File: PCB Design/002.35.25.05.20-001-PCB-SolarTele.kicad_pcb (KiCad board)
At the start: 2 copper layers, 126.7 x 46 mm, 38 parts, among them J1 Screw_Terminal_01x08, J2 Conn_01x01, J3 SMA, J4 SMA, J5 SMA, J6 SMA, J7 SMA, J8 SMA, U1 L7815, U2 L7805, U3 ADL5902ACPZ-R7, U4 LM358

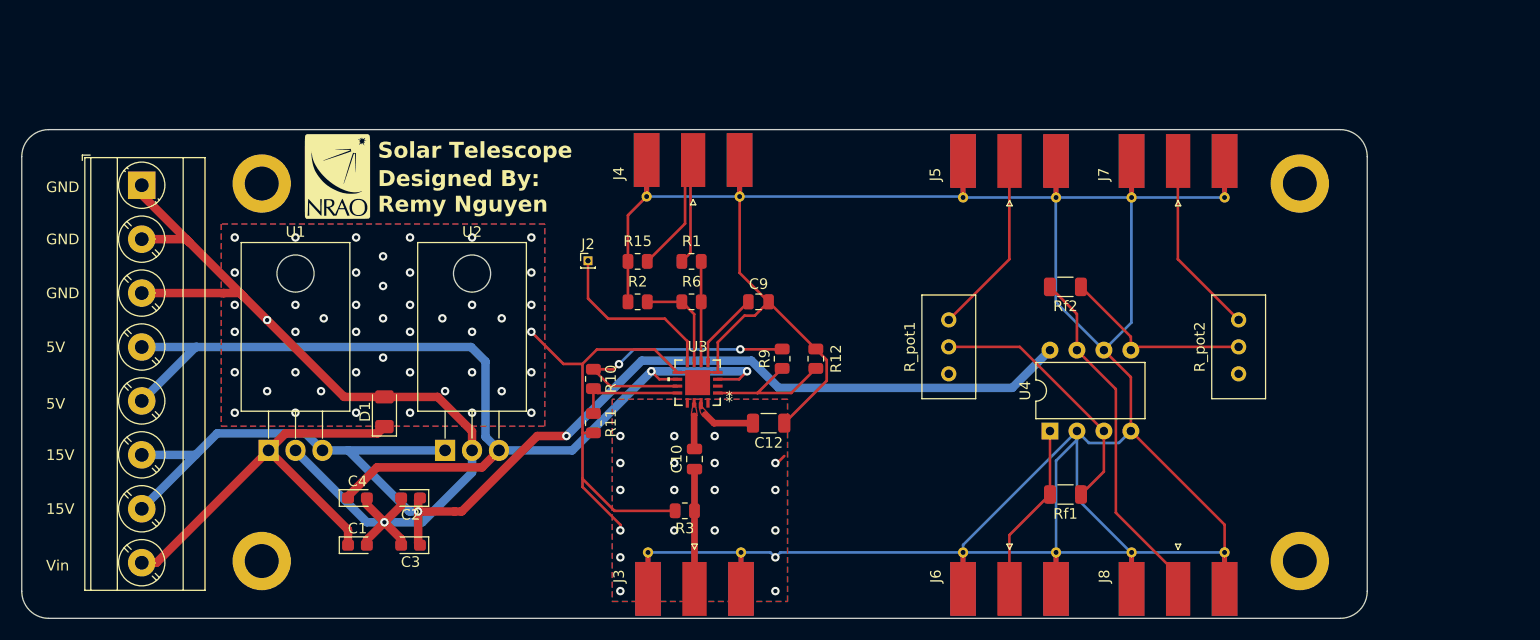
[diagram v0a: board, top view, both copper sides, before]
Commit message: Fixed SMA pad thickness
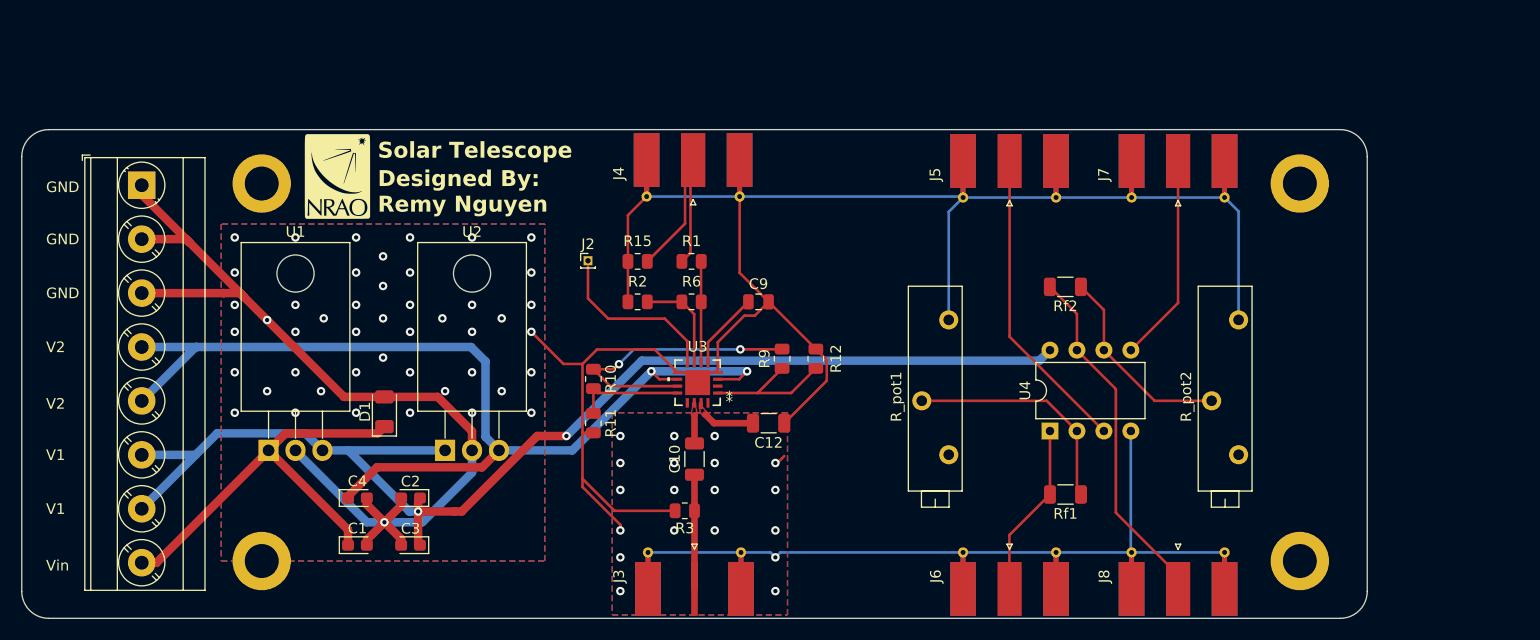
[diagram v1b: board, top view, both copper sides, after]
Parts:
- C10: footprint Capacitor_SMD:C_0805_2012Metric -> Capacitor_SMD:C_1206_3216Metric
- R_pot1, R_pot2: footprint Potentiometer_THT:Potentiometer_Bourns_3296W_Vertical -> Potentiometer_THT:Potentiometer_Bourns_3006P_Horizontal
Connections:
- R_pot1 pad 1: Net-(J5-In) -> GND
- R_pot1 pad 2: Net-(U4A-+) -> Net-(U4A--)
- R_pot2 pad 1: Net-(J7-In) -> GND
- R_pot2 pad 2: Net-(U4B-+) -> Net-(U4B--)
- Rf1 pad 1: Net-(U4A-+) -> Net-(U4A--)
- Rf2 pad 1: Net-(U4B-+) -> Net-(U4B--)
- U4 pad 2: GND -> Net-(U4A--)
- U4 pad 3: Net-(U4A-+) -> Net-(J5-In)
- U4 pad 5: Net-(U4B-+) -> Net-(J7-In)
- U4 pad 6: GND -> Net-(U4B--)
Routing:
- net GND: track 401.9 -> 334.2 mm
- net Net-(U4A-+): track 24.8 -> 0.00 mm
- net Net-(U4A--): track 0.00 -> 21.9 mm
- net Net-(U4B--): track 0.00 -> 19.0 mm
- net Net-(U4B-+): track 18.2 -> 0.00 mm
- net Net-(J5-In): track 17.3 -> 29.1 mm
- net Net-(J7-In): track 17.3 -> 19.7 mm
- net +15VDC: track 121.6 -> 119.5 mm
- net RFIN: track 11.3 -> 10.8 mm
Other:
- board text added: "0"
- board text added: "0 mm"
- board text added: "0.0037"
- board text added: "0.01 mm"
- board text added: "0.03556 mm"
- board text added: "0.762 mm"
- board text added: "1"
- board text added: "1.1"
- board text added: "3.3"
- board text added: "3.66"
- board text added: "B.Cu"
- board text added: "B.Mask"
- board text added: "B.Paste"
- board text added: "B.Silkscreen"
- board text added: "Bottom Silk Screen"
- board text added: "Bottom Solder Mask"
- board text added: "Bottom Solder Paste"
- board text added: "Color"
- board text added: "Dielectric 1"
- board text added: "Epsilon R"
- board text added: "F.Cu"
- board text added: "F.Mask"
- board text added: "F.Paste"
- board text added: "F.Silkscreen"
- board text added: "FR4 natural"
- board text added: "Green"
- board text added: "Layer Name"
- board text added: "Liquid Ink"
- board text added: "Liquid Photo"
- board text added: "Loss Tangent"
- board text added: "Material"
- board text added: "RO4350B"
- board text added: "Thickness (mm)"
- board text added: "Top Silk Screen"
- board text added: "Top Solder Mask"
- board text added: "Top Solder Paste"
- board text added: "Type"
- board text added: "V1"
- board text added: "V2"
- board text added: "White"
- board text added: "copper"
- board text added: "core"
- board text removed: "15V"
- board text removed: "5V"
- board text removed: "D"

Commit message: PCB updated to Revision B, see changelog for details
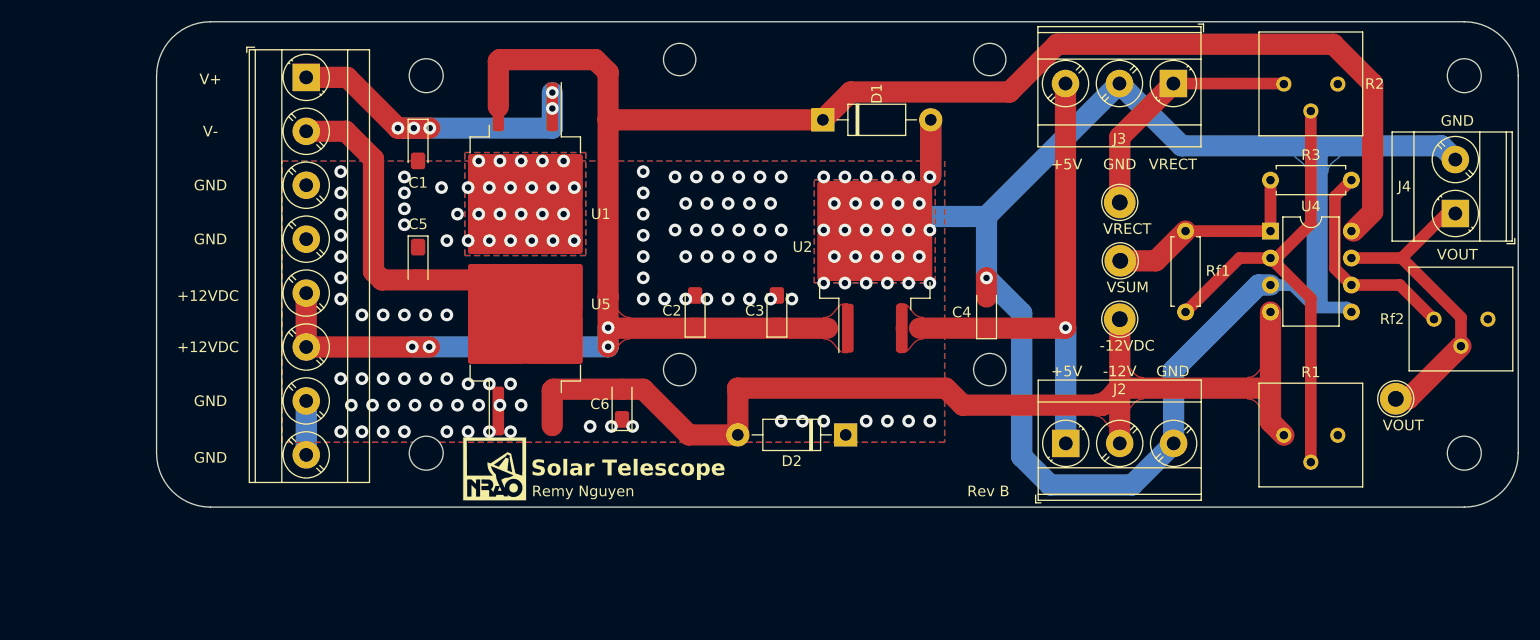
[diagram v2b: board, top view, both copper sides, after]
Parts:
- removed C10, C12: 100 pF, Capacitor_SMD:C_1206_3216Metric
- removed C9: 100 nF, Capacitor_SMD:C_0805_2012Metric
- removed the G*** at (100.8, 78.1)
- removed J5, J6, J7, J8: SMA, Connector_Coaxial:SMA_Molex_73251-1153_EdgeMount_Horizontal
- removed R10: 3.74k, Resistor_SMD:R_0805_2012Metric
- removed R11: 2k, Resistor_SMD:R_0805_2012Metric
- removed R12: 1007, Resistor_SMD:R_0805_2012Metric
- removed R15: Inf, Resistor_SMD:R_0805_2012Metric
- removed R6: 0, Resistor_SMD:R_0805_2012Metric
- removed R9: 1430, Resistor_SMD:R_0805_2012Metric
- removed R_pot1, R_pot2: 10k, Potentiometer_THT:Potentiometer_Bourns_3006P_Horizontal
- removed U3: ADL5902ACPZ-R7, imports:CP_16_20_ADI
- added -12VDC: TestPoint, TestPoint:TestPoint_Loop_D2.54mm_Drill1.5mm_Beaded, F.Cu at (174.6, 91.5)
- added C5: 2.2uF, Capacitor_Tantalum_SMD:CP_EIA-3216-10_Kemet-I_Pad1.58x1.35mm_HandSolder, F.Cu at (108.5, 86.2)
- added C6: 1uF, Capacitor_Tantalum_SMD:CP_EIA-3216-10_Kemet-I_Pad1.58x1.35mm_HandSolder, F.Cu at (127.7, 99.5)
- added D2: 1N4001, Diode_THT:D_DO-41_SOD81_P10.16mm_Horizontal, F.Cu at (148.7, 102.4)
- added G***: LOGO, footprints.pretty:nrao1_6mm_inv_silk, F.Cu at (115.7, 105.6)
- added REF**: ADL5902-EVALZ, footprints:ADL5902-EVALZ, F.Cu at (129.9, 81.7)
- added U5: L7912, Package_TO_SOT_SMD:TO-263-2, F.Cu at (118.6, 92.5)
- added VOUT: TestPoint, TestPoint:TestPoint_Loop_D2.54mm_Drill1.5mm_Beaded, F.Cu at (200.6, 99.0)
- added VRECT: TestPoint, TestPoint:TestPoint_Loop_D2.54mm_Drill1.5mm_Beaded, F.Cu at (174.6, 80.5)
- added VSUM: TestPoint, TestPoint:TestPoint_Loop_D2.54mm_Drill1.5mm_Beaded, F.Cu at (174.6, 86.0)
- C1, C2, C3, C4: footprint Capacitor_Tantalum_SMD:CP_EIA-2012-12_Kemet-R -> Capacitor_Tantalum_SMD:CP_EIA-3216-10_Kemet-I_Pad1.58x1.35mm_HandSolder
- D1: value D_Zener -> 1N4001; footprint Diode_SMD:D_1206_3216Metric -> Diode_THT:D_DO-41_SOD81_P10.16mm_Horizontal
- J2: value Conn_01x01 -> Screw_Terminal_01x03; footprint Connector_PinHeader_1.00mm:PinHeader_1x01_P1.00mm_Vertical -> TerminalBlock_Phoenix:TerminalBlock_Phoenix_MKDS-3-3-5.08_1x03_P5.08mm_Horizontal
- J3: value SMA -> Screw_Terminal_01x03; footprint Connector_Coaxial:SMA_Molex_73251-1153_EdgeMount_Horizontal -> TerminalBlock_Phoenix:TerminalBlock_Phoenix_MKDS-3-3-5.08_1x03_P5.08mm_Horizontal
- J4: value SMA -> Screw_Terminal_01x02; footprint Connector_Coaxial:SMA_Molex_73251-1153_EdgeMount_Horizontal -> TerminalBlock_Phoenix:TerminalBlock_Phoenix_MKDS-3-2-5.08_1x02_P5.08mm_Horizontal
- R1: value 0 -> 50k; footprint Resistor_SMD:R_0805_2012Metric -> Potentiometer_THT:Potentiometer_Bourns_3386P_Vertical
- R2: value Inf -> 1k; footprint Resistor_SMD:R_0805_2012Metric -> Potentiometer_THT:Potentiometer_Bourns_3386P_Vertical
- R3: value 60.3 -> 510; footprint Resistor_SMD:R_0805_2012Metric -> Resistor_THT:R_Axial_DIN0207_L6.3mm_D2.5mm_P7.62mm_Horizontal
- REF: renamed from REF**; value MountingHole_3.2mm_M3_ISO14580_Pad -> MountingHole_3.2mm_M3_ISO14580; footprint MountingHole:MountingHole_3.2mm_M3_ISO14580_Pad -> MountingHole:MountingHole_3.2mm_M3_ISO14580
- REF** (x3): value MountingHole_3.2mm_M3_ISO14580_Pad -> MountingHole_3.2mm_M3_ISO14580; footprint MountingHole:MountingHole_3.2mm_M3_ISO14580_Pad -> MountingHole:MountingHole_3.2mm_M3_ISO14580
- Rf1: value 10k -> 510; footprint Resistor_SMD:R_1206_3216Metric -> Resistor_THT:R_Axial_DIN0207_L6.3mm_D2.5mm_P7.62mm_Horizontal
- Rf2: footprint Resistor_SMD:R_1206_3216Metric -> Potentiometer_THT:Potentiometer_Bourns_3386P_Vertical
- U1: value L7815 -> L7812; footprint Package_TO_SOT_THT:TO-220-3_Horizontal_TabDown -> Package_TO_SOT_SMD:TO-263-2
- U2: footprint Package_TO_SOT_THT:TO-220-3_Horizontal_TabDown -> Package_TO_SOT_SMD:TO-263-2
- moved J4 71.9 mm to (206.2, 81.6), turned to 90 degrees
- moved J3 64.3 mm to (179.6, 69.3), turned to 180 degrees
- moved R2 64.2 mm to (190.0, 69.4), turned to -90 degrees
- moved R3 63.4 mm to (188.8, 78.4), turned to 0 degrees
- moved C4 61.8 mm to (162.0, 90.9), turned to 90 degrees
- moved R1 58.2 mm to (190.0, 102.4), turned to -90 degrees
- moved D1 49.6 mm to (146.6, 72.7), turned to 0 degrees
- moved J2 48.2 mm to (169.5, 103.2)
- moved U2 44.8 mm to (151.5, 84.7), turned to 90 degrees
- moved C3 41.0 mm to (142.3, 90.7), turned to 90 degrees
- moved C1 38.1 mm to (108.5, 75.2), turned to -90 degrees
- moved Rf2 34.9 mm to (204.2, 91.5), turned to -90 degrees
- moved U1 34.6 mm to (118.6, 79.2), turned to -90 degrees
- moved C2 32.1 mm to (134.6, 90.7), turned to 90 degrees
- moved U4 28.0 mm to (188.8, 83.2), turned to 0 degrees
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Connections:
- C1 pad 1: Vin -> V+
- C2 pad 1: +15VDC -> +12VDC
- C3 pad 1: +15VDC -> +12VDC
- D1 pad 1: Vin -> +12VDC
- J1 pad 1: GND -> V+
- J1 pad 2: GND -> V-
- J1 pad 4: +5VDC -> GND
- J1 pad 5: +5VDC -> +12VDC
- J1 pad 6: +15VDC -> +12VDC
- J1 pad 7: +15VDC -> GND
- J1 pad 8: Vin -> GND
- J2 pad 1: TEMP -> +5VDC
- J3 pad 1: RFIN -> VRECT
- J4 pad 1: DCOUT -> VOUT
- R1 pad 1: VOUT -> -12VDC
- R1 pad 2: DCOUT -> Net-(U4A--)
- R2 pad 1: GND -> VRECT
- R2 pad 2: VSET -> Net-(U4A--)
- R3 pad 1: RFIN -> VSUM
- R3 pad 2: GND -> Net-(U4B--)
- Rf1 pad 2: Net-(J6-In) -> VSUM
- Rf2 pad 2: Net-(J8-In) -> VOUT
- U1 pad 1: Vin -> V+
- U1 pad 3: +15VDC -> +12VDC
- U2 pad 1: +15VDC -> +12VDC
- U4 pad 1: Net-(J6-In) -> VSUM
- U4 pad 3: Net-(J5-In) -> GND
- U4 pad 4: GND -> -12VDC
- U4 pad 5: Net-(J7-In) -> GND
- U4 pad 7: Net-(J8-In) -> VOUT
- U4 pad 8: +15VDC -> +12VDC
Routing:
- net +12VDC: track 0.00 -> 189.7 mm, vias 0 -> 4
- net GND: track 334.2 -> 164.1 mm, vias 66 -> 142
- net +15VDC: track 119.5 -> 0.00 mm, vias 2 -> 0
- net -12VDC: track 0.00 -> 102.3 mm
- net +5VDC: track 97.6 -> 47.7 mm, vias 2 -> 1
- net Vin: track 40.2 -> 0.00 mm
- net Net-(J8-In): track 33.5 -> 0.00 mm
- net V+: track 0.00 -> 31.5 mm, vias 0 -> 5
- net V-: track 0.00 -> 30.2 mm
- net Net-(J5-In): track 29.1 -> 0.00 mm
- net VREF: track 27.1 -> 0.00 mm, vias 2 -> 0
- net Net-(U4A--): track 21.9 -> 46.7 mm
- net VRECT: track 0.00 -> 23.7 mm
- net DCOUT: track 21.6 -> 0.00 mm
- net VOUT: track 9.53 -> 30.3 mm
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- added copper zone on F.Cu, net +12VDC
- added copper zone on F.Cu, net +5VDC
- added copper zone on F.Cu, net -12VDC
- removed copper zone on F.Cu, net INHI
- removed copper zone on F.Cu, net INLO
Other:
- board size 126.7 x 46 mm -> 128.3 x 45.7 mm
- board text added: "+12VDC"
- board text added: "+5V"
- board text added: "-12V"
- board text added: "0 in"
- board text added: "0.0006 in"
- board text added: "0.0014 in"
- board text added: "0.015"
- board text added: "0.043 in / 1.10 mm"
- board text added: "0.06 in"
- board text added: "0.0640 in"
- board text added: "11.8 mil"
- board text added: "175Tg FR4"
- board text added: "2"
- board text added: "4.5"
- board text added: "5.05 in x 1.80 in"
- board text added: "7/25/2024"
- board text added: "B"
- board text added: "BOARD CHARACTERISTICS"
- board text added: "BOT-L2"
- board text added: "Board Thickness:"
- board text added: "Board overall dimensions:"
- board text added: "Castellated pads:"
- board text added: "Copper Finish:"
- board text added: "Copper Layer Count:"
- board text added: "Edge card connectors:"
- board text added: "Impedance Control:"
- board text added: "Min hole diameter:"
- board text added: "Min track width:"
- board text added: "No"
- board text added: "None"
- board text added: "Plated Board Edge:"
- board text added: "Purple"
- board text added: "Rev B"
- board text added: "TOP-L1"
- board text added: "Thickness (inches)"
- board text added: "V+"
- board text added: "V-"
- board text added: "VOUT"
- board text added: "VRECT"
- board text added: "±12V/+5V Regulator, Inverting Summer, and Inverting Amplifier"
- board text removed: "0 mm"
- board text removed: "0.0037"
- board text removed: "0.01 mm"
- board text removed: "0.03556 mm"
- board text removed: "0.762 mm"
- board text removed: "1.1"
- board text removed: "15V/5V Regulator, RF Power Detector, and Non-Inverting Amplifier"
- board text removed: "3.3"
- board text removed: "3.66"
- board text removed: "6/29/2023"
- board text removed: "Designed By: Remy Nguyen"
- board text removed: "Green"
- board text removed: "RO4350B"
- board text removed: "Thickness (mm)"
- board text removed: "V1"
- board text removed: "V2"
- board text removed: "Vin"
